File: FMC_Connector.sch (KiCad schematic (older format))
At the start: 2 parts, among them J1 ASP-134488-01

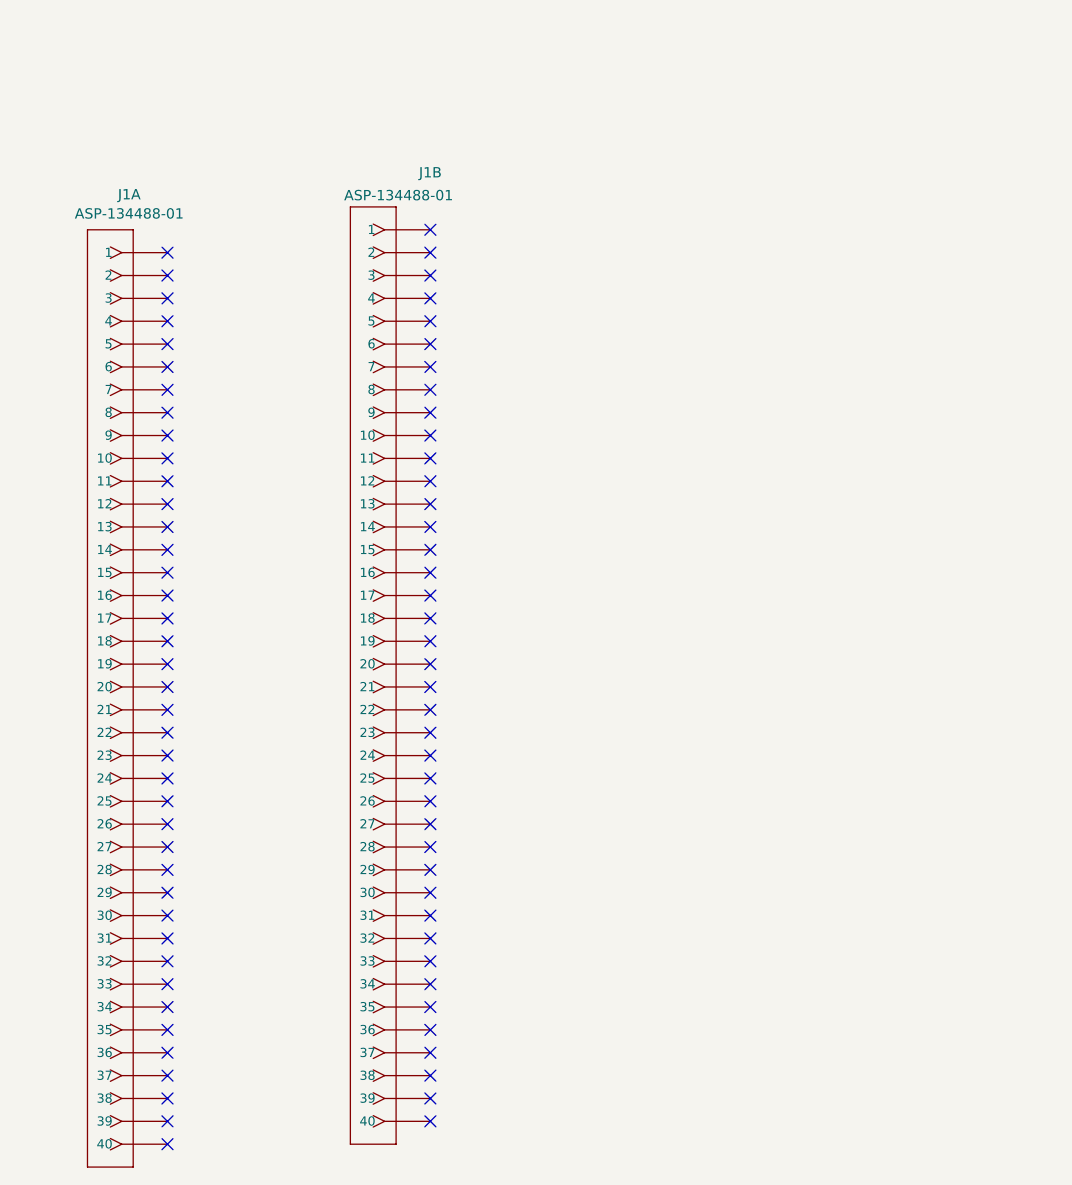
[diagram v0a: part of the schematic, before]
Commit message: Added dummy nets to FMC connector
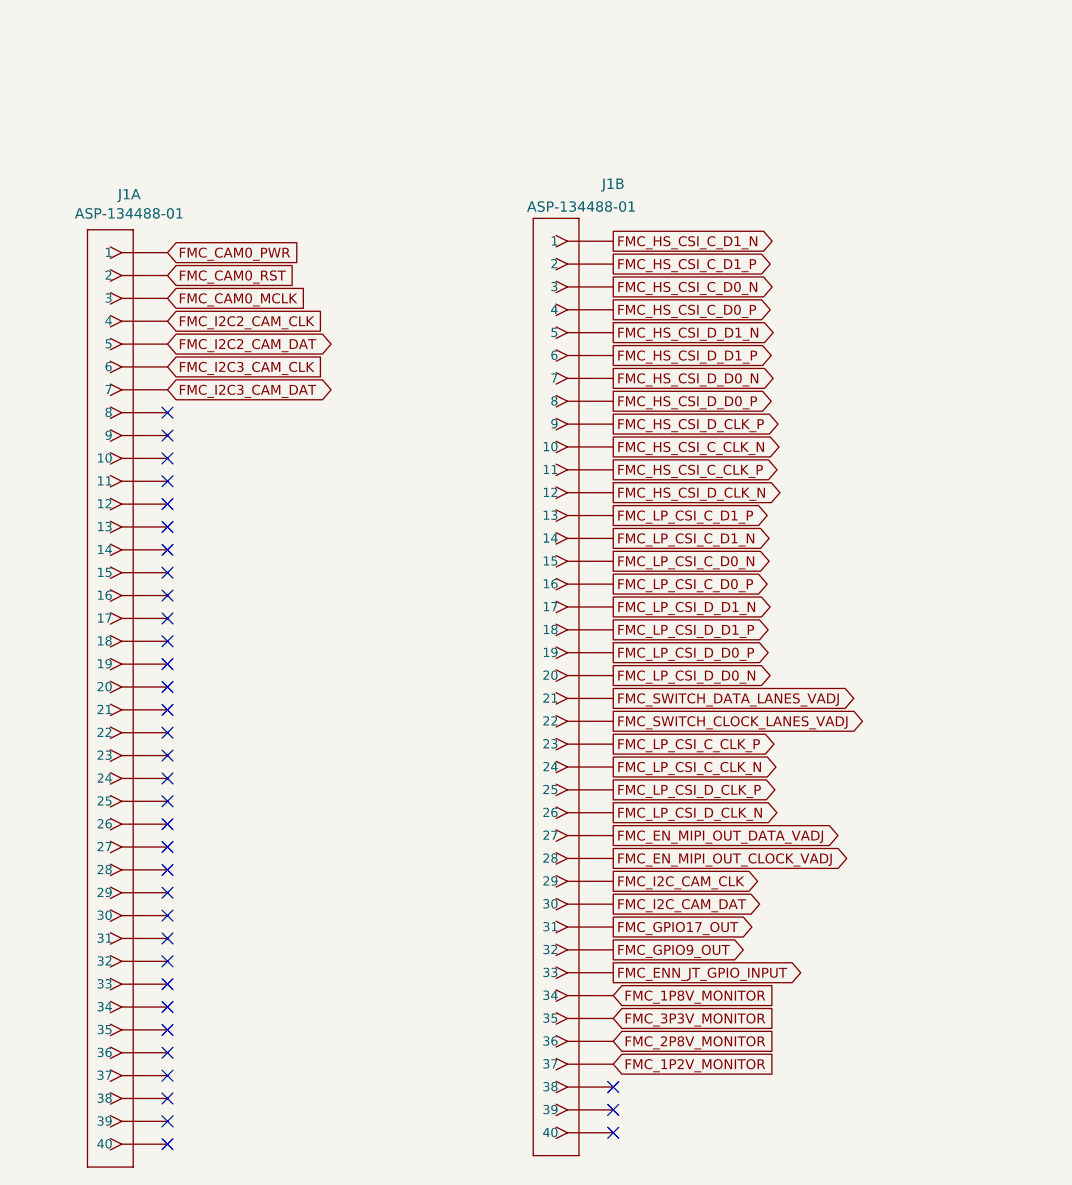
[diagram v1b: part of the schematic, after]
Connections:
- net FMC_CAM0_PWR: now reaches J1.A1 (1)
- net FMC_CAM0_RST: now reaches J1.A2 (2)
- net FMC_CAM0_MCLK: now reaches J1.A3 (3)
- net FMC_I2C2_CAM_CLK: now reaches J1.A4 (4)
- net FMC_I2C2_CAM_DAT: now reaches J1.A5 (5)
- net FMC_I2C3_CAM_CLK: now reaches J1.A6 (6)
- net FMC_I2C3_CAM_DAT: now reaches J1.A7 (7)
- net FMC_HS_CSI_C_D1_N: now reaches J1.B1 (1)
- net FMC_HS_CSI_C_CLK_N: now reaches J1.B10 (10)
- net FMC_HS_CSI_C_CLK_P: now reaches J1.B11 (11)
- net FMC_HS_CSI_D_CLK_N: now reaches J1.B12 (12)
- net FMC_LP_CSI_C_D1_P: now reaches J1.B13 (13)
- net FMC_LP_CSI_C_D1_N: now reaches J1.B14 (14)
- net FMC_LP_CSI_C_D0_N: now reaches J1.B15 (15)
- net FMC_LP_CSI_C_D0_P: now reaches J1.B16 (16)
- net FMC_LP_CSI_D_D1_N: now reaches J1.B17 (17)
- net FMC_LP_CSI_D_D1_P: now reaches J1.B18 (18)
- net FMC_LP_CSI_D_D0_P: now reaches J1.B19 (19)
- net FMC_HS_CSI_C_D1_P: now reaches J1.B2 (2)
- net FMC_LP_CSI_D_D0_N: now reaches J1.B20 (20)
- net FMC_SWITCH_DATA_LANES_VADJ: now reaches J1.B21 (21)
- net FMC_SWITCH_CLOCK_LANES_VADJ: now reaches J1.B22 (22)
- net FMC_LP_CSI_C_CLK_P: now reaches J1.B23 (23)
- net FMC_LP_CSI_C_CLK_N: now reaches J1.B24 (24)
- net FMC_LP_CSI_D_CLK_P: now reaches J1.B25 (25)
- net FMC_LP_CSI_D_CLK_N: now reaches J1.B26 (26)
- net FMC_EN_MIPI_OUT_DATA_VADJ: now reaches J1.B27 (27)
- net FMC_EN_MIPI_OUT_CLOCK_VADJ: now reaches J1.B28 (28)
- net FMC_I2C_CAM_CLK: now reaches J1.B29 (29)
- net FMC_HS_CSI_C_D0_N: now reaches J1.B3 (3)
- net FMC_I2C_CAM_DAT: now reaches J1.B30 (30)
- net FMC_GPIO17_OUT: now reaches J1.B31 (31)
- net FMC_GPIO9_OUT: now reaches J1.B32 (32)
- net FMC_ENN_JT_GPIO_INPUT: now reaches J1.B33 (33)
- net FMC_1P8V_MONITOR: now reaches J1.B34 (34)
- net FMC_3P3V_MONITOR: now reaches J1.B35 (35)
- net FMC_2P8V_MONITOR: now reaches J1.B36 (36)
- net FMC_1P2V_MONITOR: now reaches J1.B37 (37)
- net FMC_HS_CSI_C_D0_P: now reaches J1.B4 (4)
- net FMC_HS_CSI_D_D1_N: now reaches J1.B5 (5)
- net FMC_HS_CSI_D_D1_P: now reaches J1.B6 (6)
- net FMC_HS_CSI_D_D0_N: now reaches J1.B7 (7)
- net FMC_HS_CSI_D_D0_P: now reaches J1.B8 (8)
- net FMC_HS_CSI_D_CLK_P: now reaches J1.B9 (9)
- no-connect marks 304 -> 260
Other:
- moved on the sheet: J1B
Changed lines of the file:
@@
 L FMC_MIPI_v2:ASP-134488-01_VER2 J1
 U 2 1 61918832
-P 2350 8900
-F 0 "J1" H 2100 11150 45  0000 L CNN
-F 1 "ASP-134488-01" H 2050 11050 45  0000 L CNN
-F 2 "FMC_MIPI_v2_sym:ASP-134488-01_VER2" H 2350 9200 60  0001 C CNN
-F 3 "https://www.mouser.com/ProductDetail/Samtec/ASP-134488-01?qs=jyzYFa4oMQiB2Frr%252B13AUg%3D%3D" H 2350 9200 60  0001 C CNN
-	2    2350 8900
+P 3150 8950
+F 0 "J1" H 2900 11200 45  0000 L CNN
+F 1 "ASP-134488-01" H 2850 11100 45  0000 L CNN
+F 2 "FMC_MIPI_v2_sym:ASP-134488-01_VER2" H 3150 9250 60  0001 C CNN
+F 3 "https://www.mouser.com/ProductDetail/Samtec/ASP-134488-01?qs=jyzYFa4oMQiB2Frr%252B13AUg%3D%3D" H 3150 9250 60  0001 C CNN
+	2    3150 8950
 	-1   0    0    -1
 $EndComp
@@
 	1    0    0    -1
 $EndComp
-NoConn ~ 1400 7000
-NoConn ~ 1400 7100
-NoConn ~ 1400 7200
-NoConn ~ 1400 7300
-NoConn ~ 1400 7400
-NoConn ~ 1400 7500
-NoConn ~ 1400 7600
 NoConn ~ 1400 7700
 NoConn ~ 1400 7800
@@
 NoConn ~ 1400 10800
 NoConn ~ 1400 10900
-NoConn ~ 2550 6900
-NoConn ~ 2550 7000
-NoConn ~ 2550 7100
-NoConn ~ 2550 7200
-NoConn ~ 2550 7300
-NoConn ~ 2550 7400
-NoConn ~ 2550 7500
-NoConn ~ 2550 7600
-NoConn ~ 2550 7700
-NoConn ~ 2550 7800
-NoConn ~ 2550 7900
-NoConn ~ 2550 8000
-NoConn ~ 2550 8100
-NoConn ~ 2550 8200
-NoConn ~ 2550 8300
-NoConn ~ 2550 8400
-NoConn ~ 2550 8500
-NoConn ~ 2550 8600
-NoConn ~ 2550 8700
-NoConn ~ 2550 8800
-NoConn ~ 2550 8900
-NoConn ~ 2550 9000
-NoConn ~ 2550 9100
-NoConn ~ 2550 9200
-NoConn ~ 2550 9300
-NoConn ~ 2550 9400
-NoConn ~ 2550 9500
-NoConn ~ 2550 9600
-NoConn ~ 2550 9700
-NoConn ~ 2550 9800
-NoConn ~ 2550 9900
-NoConn ~ 2550 10000
-NoConn ~ 2550 10100
-NoConn ~ 2550 10200
-NoConn ~ 2550 10300
-NoConn ~ 2550 10400
-NoConn ~ 2550 10500
-NoConn ~ 2550 10600
-NoConn ~ 2550 10700
-NoConn ~ 2550 10800
 NoConn ~ 14800 1200
 NoConn ~ 14800 1300
@@
 NoConn ~ 6200 3350
 NoConn ~ 6200 3150
-NoConn ~ 6200 3050
 NoConn ~ 6200 2850
 NoConn ~ 6200 2750
@@
 Text Label 10600 4950 0    50   ~ 0
 VDD_VADJ
+Text GLabel 3350 6950 2    43   Output ~ 0
+FMC_HS_CSI_C_D1_N
+Text GLabel 3350 7050 2    43   Output ~ 0
+FMC_HS_CSI_C_D1_P
+Text GLabel 3350 7150 2    43   Output ~ 0
+FMC_HS_CSI_C_D0_N
+Text GLabel 3350 7250 2    43   Output ~ 0
+FMC_HS_CSI_C_D0_P
+Text GLabel 3350 7350 2    43   Output ~ 0
+FMC_HS_CSI_D_D1_N
+Text GLabel 3350 7450 2    43   Output ~ 0
+FMC_HS_CSI_D_D1_P
+Text GLabel 3350 7550 2    43   Output ~ 0
+FMC_HS_CSI_D_D0_N
+Text GLabel 3350 7650 2    43   Output ~ 0
+FMC_HS_CSI_D_D0_P
+Text GLabel 3350 7750 2    43   Output ~ 0
+FMC_HS_CSI_D_CLK_P
+Text GLabel 3350 7850 2    43   Output ~ 0
+FMC_HS_CSI_C_CLK_N
+Text GLabel 3350 7950 2    43   Output ~ 0
+FMC_HS_CSI_C_CLK_P
+Text GLabel 3350 8050 2    43   Output ~ 0
+FMC_HS_CSI_D_CLK_N
+Text GLabel 3350 8150 2    43   Output ~ 0
+FMC_LP_CSI_C_D1_P
+Text GLabel 3350 8250 2    43   Output ~ 0
+FMC_LP_CSI_C_D1_N
+Text GLabel 3350 8350 2    43   Output ~ 0
+FMC_LP_CSI_C_D0_N
+Text GLabel 3350 8450 2    43   Output ~ 0
+FMC_LP_CSI_C_D0_P
+Text GLabel 3350 8550 2    43   Output ~ 0
+FMC_LP_CSI_D_D1_N
+Text GLabel 3350 8650 2    43   Output ~ 0
+FMC_LP_CSI_D_D1_P
+Text GLabel 3350 8750 2    43   Output ~ 0
+FMC_LP_CSI_D_D0_P
+Text GLabel 3350 8850 2    43   Output ~ 0
+FMC_LP_CSI_D_D0_N
+Text GLabel 3350 8950 2    43   Output ~ 0
+FMC_SWITCH_DATA_LANES_VADJ
+Text GLabel 3350 9050 2    43   Output ~ 0
+FMC_SWITCH_CLOCK_LANES_VADJ
+Text GLabel 3350 9150 2    43   Output ~ 0
+FMC_LP_CSI_C_CLK_P
+Text GLabel 3350 9250 2    43   Output ~ 0
+FMC_LP_CSI_C_CLK_N
+Text GLabel 3350 9350 2    43   Output ~ 0
+FMC_LP_CSI_D_CLK_P
+Text GLabel 3350 9450 2    43   Output ~ 0
+FMC_LP_CSI_D_CLK_N
+Text GLabel 3350 9550 2    43   Output ~ 0
+FMC_EN_MIPI_OUT_DATA_VADJ
+Text GLabel 3350 9650 2    43   Output ~ 0
+FMC_EN_MIPI_OUT_CLOCK_VADJ
+Text GLabel 3350 9750 2    43   Output ~ 0
+FMC_I2C_CAM_CLK
+Text GLabel 3350 9850 2    43   Output ~ 0
+FMC_I2C_CAM_DAT
+Text GLabel 3350 9950 2    43   Output ~ 0
+FMC_GPIO17_OUT
+Text GLabel 3350 10050 2    43   Output ~ 0
+FMC_GPIO9_OUT
+Text GLabel 1400 7000 2    43   Input ~ 0
+FMC_CAM0_PWR
+Text GLabel 1400 7100 2    43   Input ~ 0
+FMC_CAM0_RST
+Text GLabel 1400 7200 2    43   Input ~ 0
+FMC_CAM0_MCLK
+Text GLabel 1400 7300 2    43   Input ~ 0
+FMC_I2C2_CAM_CLK
+Text GLabel 1400 7400 2    43   BiDi ~ 0
+FMC_I2C2_CAM_DAT
+Text GLabel 1400 7500 2    43   Input ~ 0
+FMC_I2C3_CAM_CLK
+Text GLabel 1400 7600 2    43   BiDi ~ 0
+FMC_I2C3_CAM_DAT
+Text GLabel 3350 10250 2    43   Input ~ 0
+FMC_1P8V_MONITOR
+Text GLabel 3350 10150 2    43   Output ~ 0
+FMC_ENN_JT_GPIO_INPUT
+Text GLabel 3350 10550 2    43   Input ~ 0
+FMC_1P2V_MONITOR
+Text GLabel 3350 10450 2    43   Input ~ 0
+FMC_2P8V_MONITOR
+Text GLabel 3350 10350 2    43   Input ~ 0
+FMC_3P3V_MONITOR
+NoConn ~ 6200 3050
+NoConn ~ 3350 10650
+NoConn ~ 3350 10750
+NoConn ~ 3350 10850
 $EndSCHEMATC

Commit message: started routing
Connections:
- wire segments 189 -> 242
- no-connect marks 260 -> 207
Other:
- note added: "Move CSI D clock here"
- note added: "Total 44 lines in use, 6 diff pairs (12 lines)"
- moved on the sheet: J1C, J1D, J1E, J1F, R18
